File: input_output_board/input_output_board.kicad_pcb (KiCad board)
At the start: 2 copper layers, 150 x 50 mm, 25 parts, among them J1 Neutrik_NCJ6FA-H, J2 Neutrik_NCJ6FA-H, J3 Neutrik_NCJ6FA-H, J4 Neutrik_NCJ6FA-H, J5 AudioJack3, J6 Conn_02x05_Odd_Even, J7 Molex_SL_01x02_Male, J8 Molex_SL_01x02_Male, K1 G6S-2, K2 G6S-2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

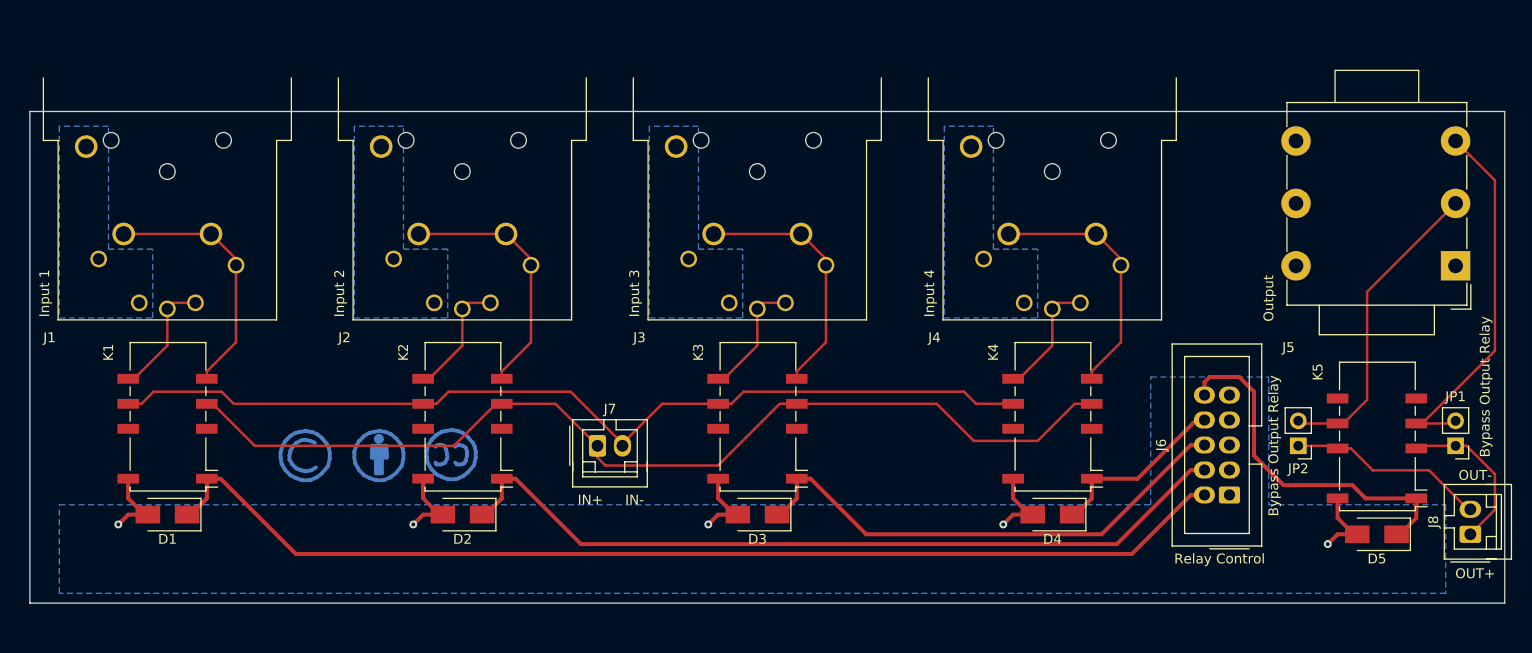
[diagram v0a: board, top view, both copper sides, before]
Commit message: Update layout of input/output board
- remove jumpers to bypass output relay. Jumper wires can be soldered
onto relay footprint instead.
- layout of output connectors complete
- still need to finalize output connector choice & placement
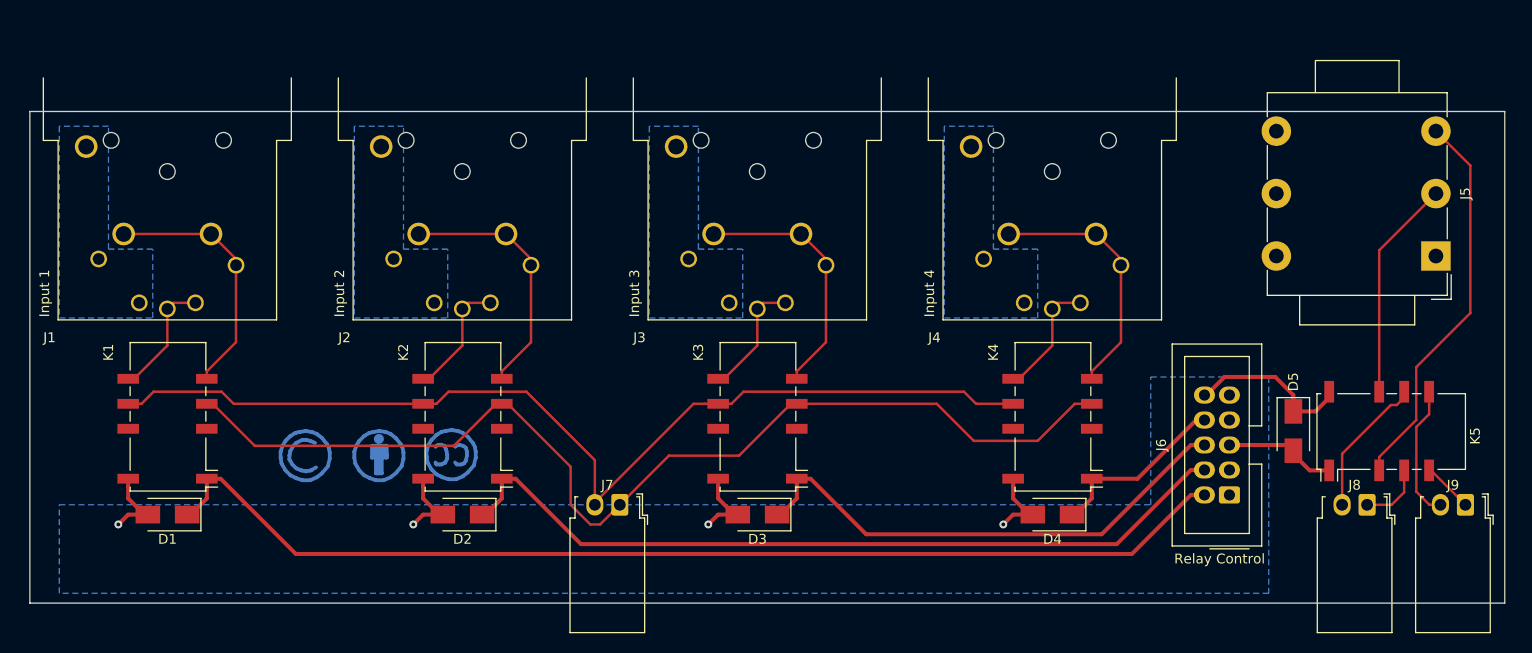
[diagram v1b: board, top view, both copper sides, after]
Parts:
- removed JP1, JP2: Jumper_NO_Small, Connector_PinHeader_2.54mm:PinHeader_1x02_P2.54mm_Vertical
- added J9: Molex_SL_01x02_Male, Connector_Molex_SL:Molex_SL_A-70553-0001_1x02_P2.54mm_Horizontal, F.Cu at (196.0, 140.0)
- J7, J8: footprint Connector_Molex_SL:Molex_SL_A-70543-0001_1x02_P2.54mm_Vertical -> Connector_Molex_SL:Molex_SL_A-70553-0001_1x02_P2.54mm_Horizontal
- moved D5 13.5 mm to (178.5, 132.5), turned to 270 degrees
- moved J8 10.9 mm to (186.0, 140.0), turned to 180 degrees
- moved J7 6.42 mm to (110.0, 140.0), turned to 180 degrees
- moved J5 2.24 mm to (193.0, 102.0)
- moved K5 1.58 mm to (188.5, 132.5), turned to 90 degrees
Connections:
- D5 pad 1: /output_mute_select -> /headphone_select
- J5 pad R: Net-(J5-PadR) -> /main_cold
- J5 pad T: Net-(J5-PadT) -> /main_hot
- J6 pad 10: /output_mute_select -> /headphone_select
- K5 pad 1: /output_mute_select -> GNDRELAY
- K5 pad 10: /output_cold -> /main_cold
- K5 pad 12: GNDRELAY -> /headphone_select
- K5 pad 3: /output_hot -> /main_hot
- K5 pad 4: Net-(J5-PadT) -> /output_hot
- K5 pad 5: Net-(K5-Pad5) -> /headphone_hot
- K5 pad 8: Net-(K5-Pad8) -> /headphone_cold
- K5 pad 9: Net-(J5-PadR) -> /output_cold
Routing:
- net /main_hot: track 0.00 -> 39.8 mm
- net Net-(J5-PadT): track 38.2 -> 0.00 mm
- net /output_mute_select: track 36.7 -> 0.00 mm
- net Net-(J5-PadR): track 31.8 -> 0.00 mm
- net /main_cold: track 0.00 -> 22.5 mm
- net /headphone_select: track 0.00 -> 17.1 mm
- net /headphone_cold: track 0.00 -> 13.7 mm
- net /output_hot: track 16.5 -> 6.53 mm
- net /input_selected_cold: track 96.6 -> 104.4 mm
- net /input_selected_hot: track 102.6 -> 109.1 mm
- net /output_cold: track 20.2 -> 14.5 mm
- net /headphone_hot: track 0.00 -> 5.14 mm
- net GNDRELAY: track 40.5 -> 43.8 mm, vias 5 -> 4
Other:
- board text added: "TODO arrange so first input is closest to output check output jack footprint align output jack with input jack make sure all jacks are properly positioned adjust location of relay connector output jack 3d model fix placement on output internal audio connector (and maybe input as well) -- right angle connectors? Move output relay? resize board if necessary adjust GNDD plane update silk/page date a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"
- board text removed: "TODO arrange so first input is closest to output check output jack footprint align output jack with input jack make sure all jacks are properly positioned fix placement of output relay bypass jumpers adjust location of relay connector output jack 3d model fix placement on output internal audio connector (and maybe input as well) -- right angle connectors? Move output relay? resize board if necess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"

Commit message: update schematic & layout so output connector is same as input connectors
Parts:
- J5: value AudioJack3 -> Neutrik_NCJ6FA-H; footprint Connector_Audio:Jack_3.5mm_Neutrik_NMJ6HCD2_Horizontal -> Connector_Audio_gkeeth:Jack_Combo_Neutrik_NCJ6FA-H_Horizontal
- moved J5 20.6 mm to (177.0, 115.0), turned to 0 degrees
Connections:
- J5 pad S: /output_shield -> /main_shield
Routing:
- net /main_cold: track 22.5 -> 12.3 mm
- net /main_hot: track 39.8 -> 35.5 mm
- added copper zone on B.Cu, net /main_shield
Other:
- board text added: "TODO use upstream footprints arrange so first input is closest to output make sure all jacks are properly positioned adjust location of relay connector output jack 3d model fix placement on output internal audio connector (and maybe input as well) -- right angle connectors? Move output relay? resize board if necessary adjust GNDD plane update silk/page date add mounting holes"
- board text removed: "TODO arrange so first input is closest to output check output jack footprint align output jack with input jack make sure all jacks are properly positioned adjust location of relay connector output jack 3d model fix placement on output internal audio connector (and maybe input as well) -- right angle connectors? Move output relay? resize board if necessary adjust GNDD plane update silk/page date a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"

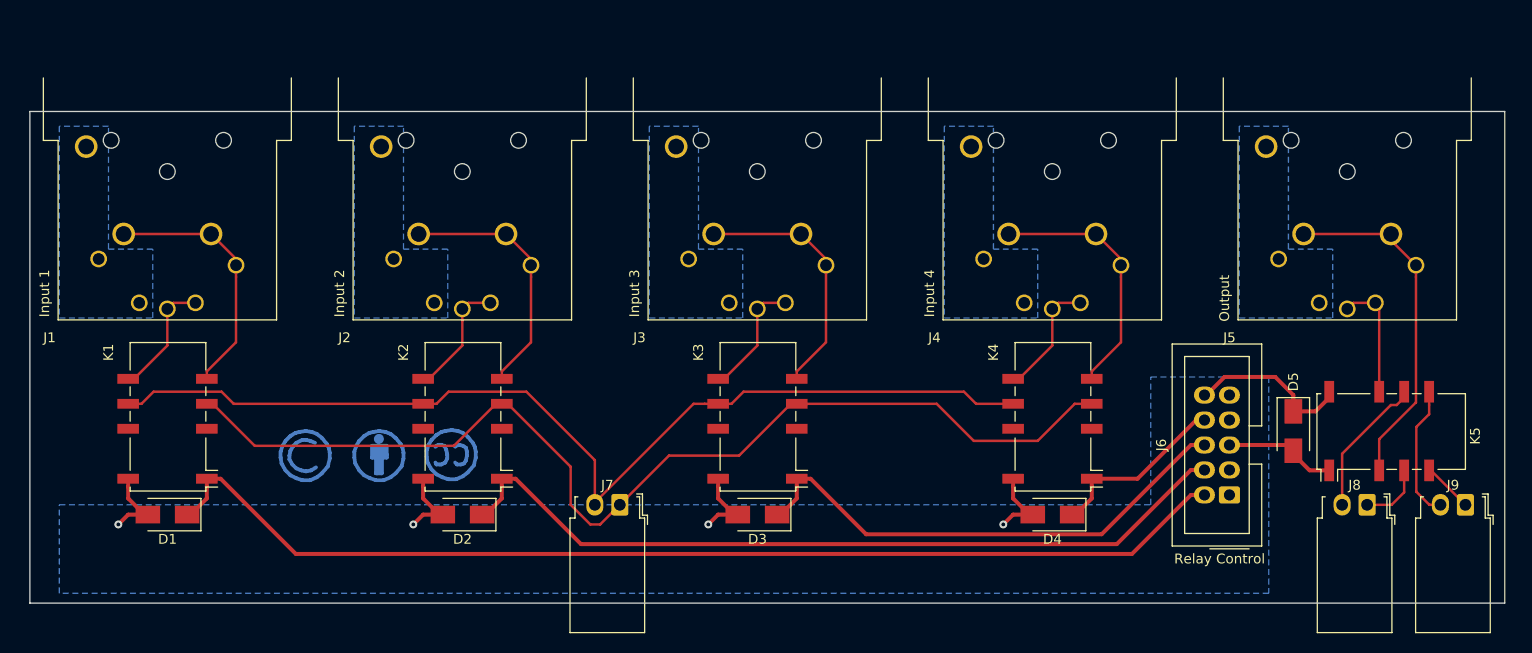
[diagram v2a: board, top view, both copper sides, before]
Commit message: update jack footprints in layout to project-local footprints from upstream pull request
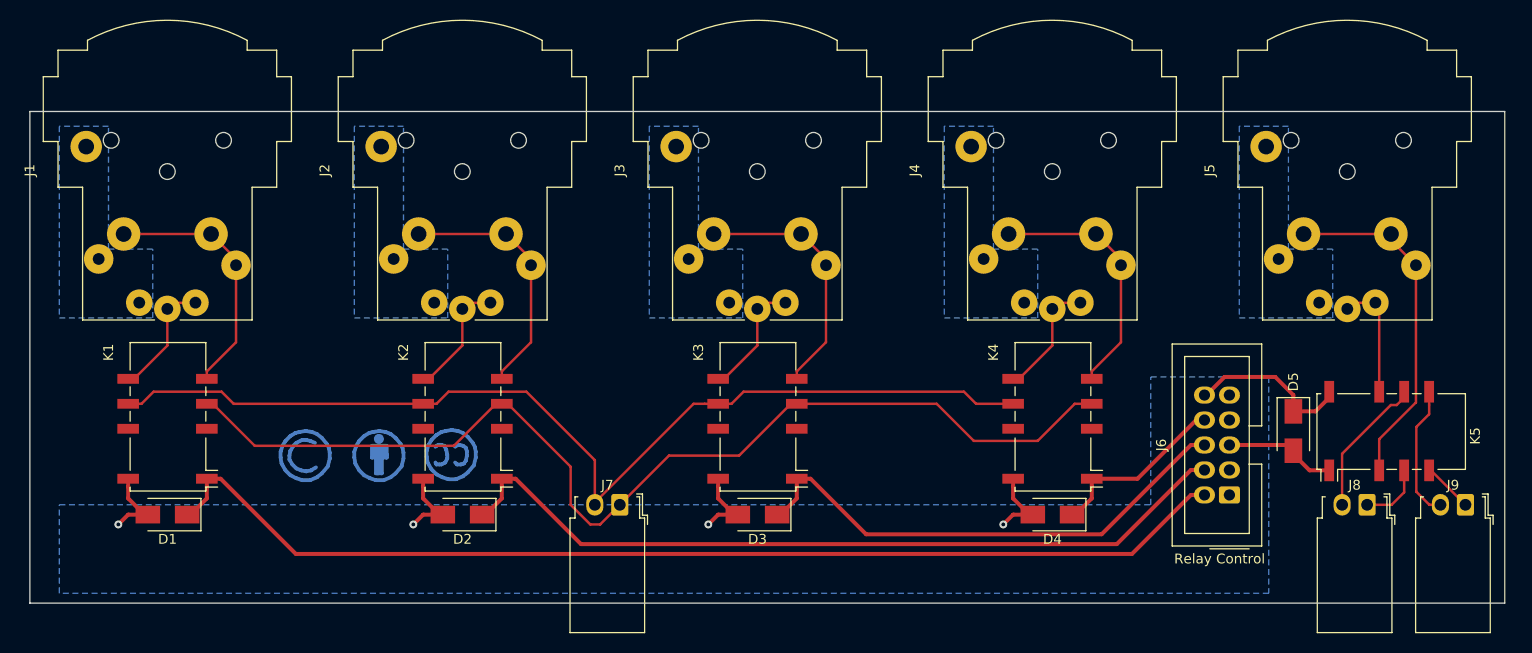
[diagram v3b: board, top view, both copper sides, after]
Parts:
- J1, J2, J3, J4, J5: value Neutrik_NCJ6FA-H -> Neutrik_NCJ6FA-H-0; footprint Connector_Audio_gkeeth:Jack_Combo_Neutrik_NCJ6FA-H_Horizontal -> Connector_Audio_project:Jack_XLR-6.35mm_Neutrik_NCJ6FA-H-0_Horizontal
- turned J1 to 90 degrees
- turned J2 to 90 degrees
- turned J3 to 90 degrees
- turned J4 to 90 degrees
- turned J5 to 90 degrees

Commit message: move input/output connectors to line up with board edge, change output connector to XLR, adjust relay ground plane
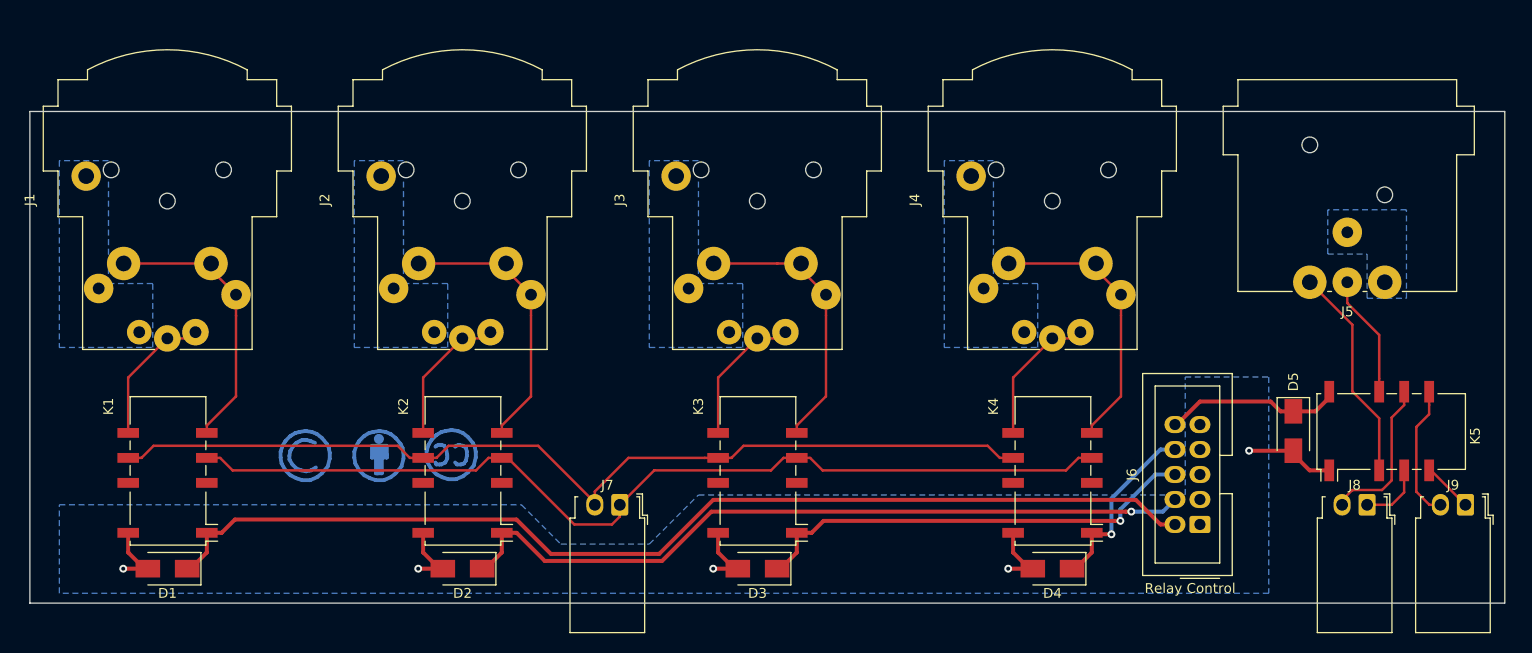
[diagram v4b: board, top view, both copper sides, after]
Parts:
- J5: value Neutrik_NCJ6FA-H-0 -> Neutrik_NC3MAH; footprint Connector_Audio_project:Jack_XLR-6.35mm_Neutrik_NCJ6FA-H-0_Horizontal -> Connector_Audio_project:Jack_XLR_Neutrik_NC3MAH_Horizontal
- moved J5 11.1 mm to (187.8, 117.4), turned to 180 degrees
- moved D1 5.50 mm to (64.0, 146.5)
- moved D2 5.50 mm to (94.0, 146.5)
- moved D3 5.50 mm to (124.0, 146.5)
- moved D4 5.50 mm to (154.0, 146.5)
- moved K1 5.50 mm to (64.0, 136.5)
- moved K2 5.50 mm to (94.0, 136.5)
- moved K3 5.50 mm to (124.0, 136.5)
- moved K4 5.50 mm to (154.0, 136.5)
- moved J6 4.24 mm to (169.0, 142.0)
- moved J1 3.00 mm to (57.0, 118.0)
- moved J2 3.00 mm to (87.0, 118.0)
- moved J3 3.00 mm to (117.0, 118.0)
- moved J4 3.00 mm to (147.0, 118.0)
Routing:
- net /main_hot: track 35.5 -> 22.1 mm
- net /input_selected_hot: track 109.1 -> 98.4 mm
- net /input_selected_cold: track 104.4 -> 97.9 mm
- net /input3_select: track 52.2 -> 46.5 mm, vias 0 -> 1
- net GNDRELAY: track 43.8 -> 38.5 mm, vias 4 -> 5
- net /input2_select: track 82.0 -> 76.9 mm, vias 0 -> 1
- net /input1_select: track 111.8 -> 108.5 mm
- net /input4_hot: track 25.9 -> 28.4 mm
- net /input3_hot: track 25.9 -> 28.4 mm
- net /input2_hot: track 25.9 -> 28.4 mm
- net /input1_hot: track 25.9 -> 28.4 mm
- net /input4_cold: track 12.2 -> 14.4 mm
- net /input3_cold: track 12.2 -> 14.4 mm
- net /input2_cold: track 12.2 -> 14.4 mm
- net /input1_cold: track 12.2 -> 14.4 mm
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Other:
- net class shield: clearance 0.3556 -> 0.3048
- board text added: "TODO arrange so first input is closest to output fix placement on output internal audio connector (and maybe input as well) Move output relay? make 3d models for right angle connectors update silk/page date"
- board text removed: "TODO use upstream footprints arrange so first input is closest to output make sure all jacks are properly positioned adjust location of relay connector output jack 3d model fix placement on output internal audio connector (and maybe input as well) -- right angle connectors? Move output relay? resize board if necessary adjust GNDD plane update silk/page date add mounting holes"

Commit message: finalize layout based on schematic. Add silk/fab labels to connectors
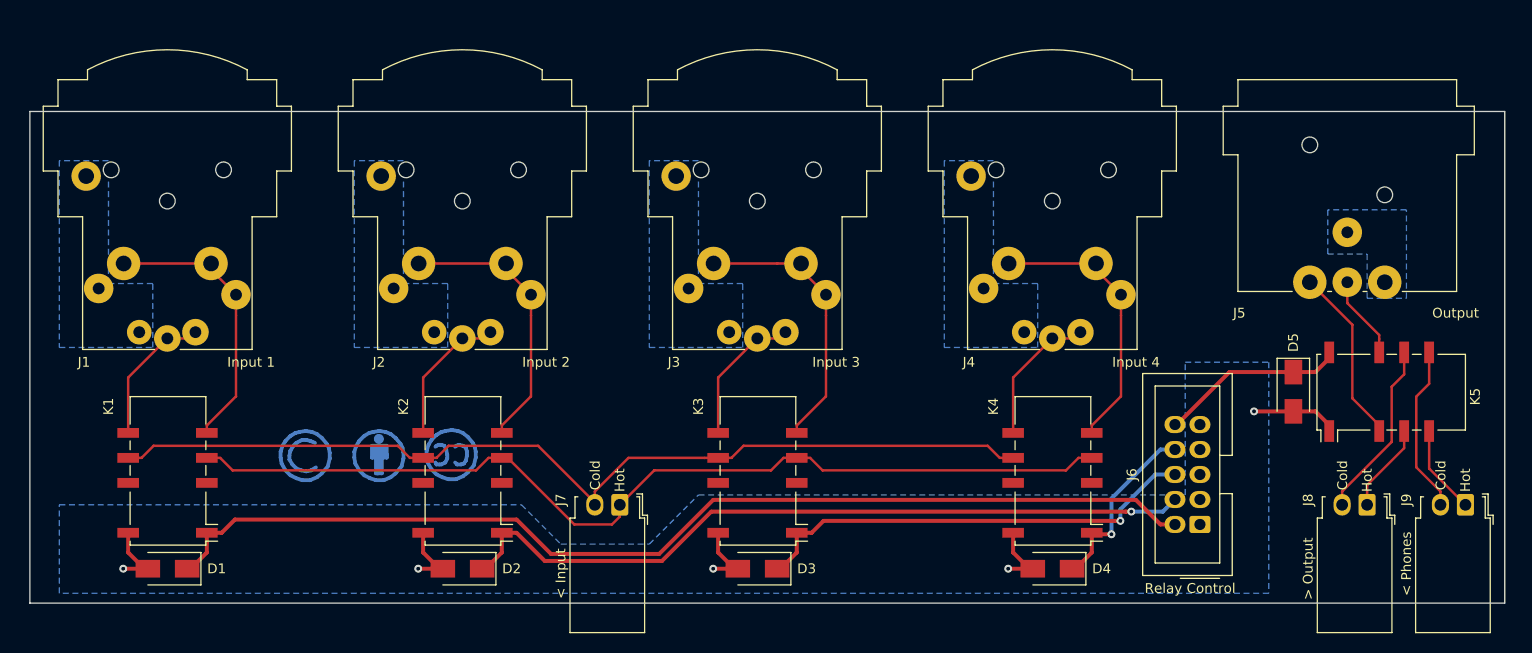
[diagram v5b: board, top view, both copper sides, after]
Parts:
- moved D5 4.00 mm to (178.5, 128.5)
- moved K5 4.00 mm to (188.5, 128.5)
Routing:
- net /main_hot: track 22.1 -> 18.1 mm
- net /main_cold: track 12.5 -> 8.48 mm
- net /headphone_hot: track 5.14 -> 9.03 mm
- net /headphone_cold: track 13.7 -> 17.1 mm
- net /output_hot: track 6.53 -> 9.06 mm
- net /output_cold: track 15.9 -> 18.1 mm
- net /headphone_select: track 18.5 -> 19.3 mm
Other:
- board text added: "Input/Output Board rev0 Preamp 2019 G. Keeth 2019-09-22"
- board text removed: "Input/Output Board rev0 Preamp 2019 G. Keeth 2019-06-21"
- board text removed: "TODO arrange so first input is closest to output fix placement on output internal audio connector (and maybe input as well) Move output relay? make 3d models for right angle connectors update silk/page date"
